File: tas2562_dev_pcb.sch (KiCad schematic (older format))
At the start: 24 parts, among them J1 Conn_01x10_Female, J2 ADDR, J3 Screw_Terminal_01x02, J4 Conn_01x10_Female, U1 LM1117-1.8, U2 TAS2562

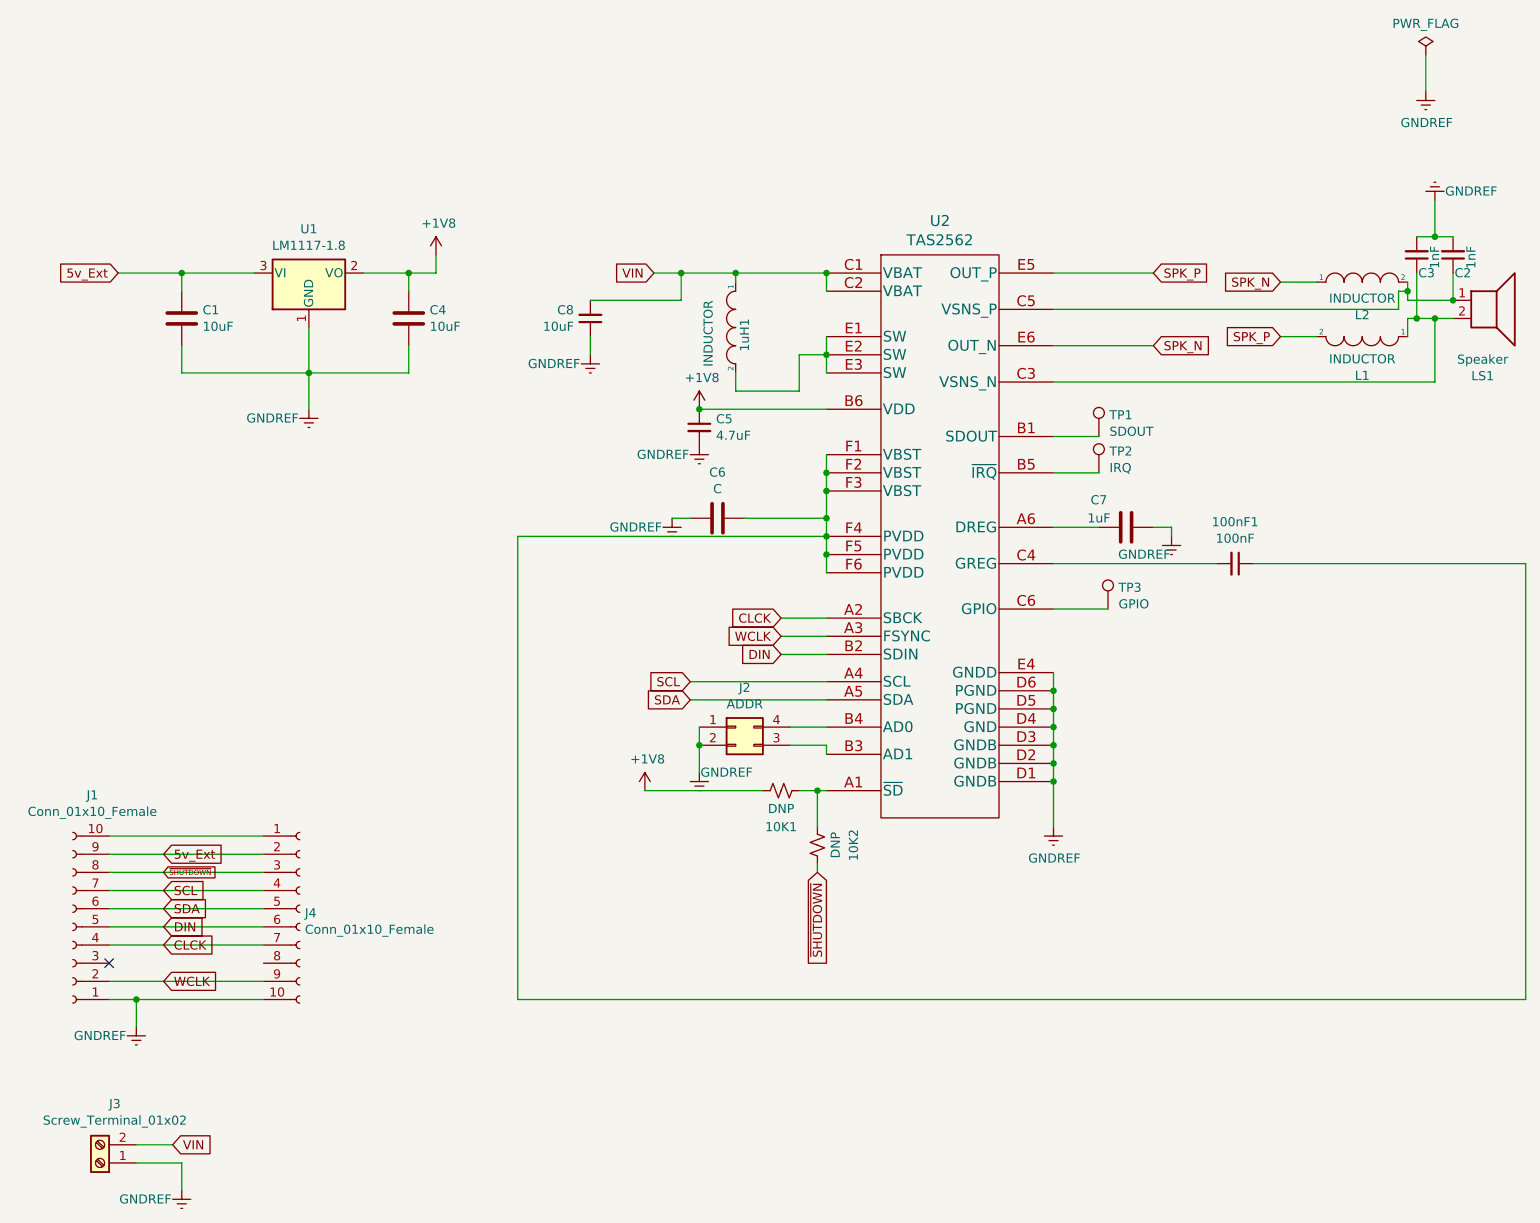
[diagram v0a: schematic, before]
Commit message: added gerber, layout done in 2layers
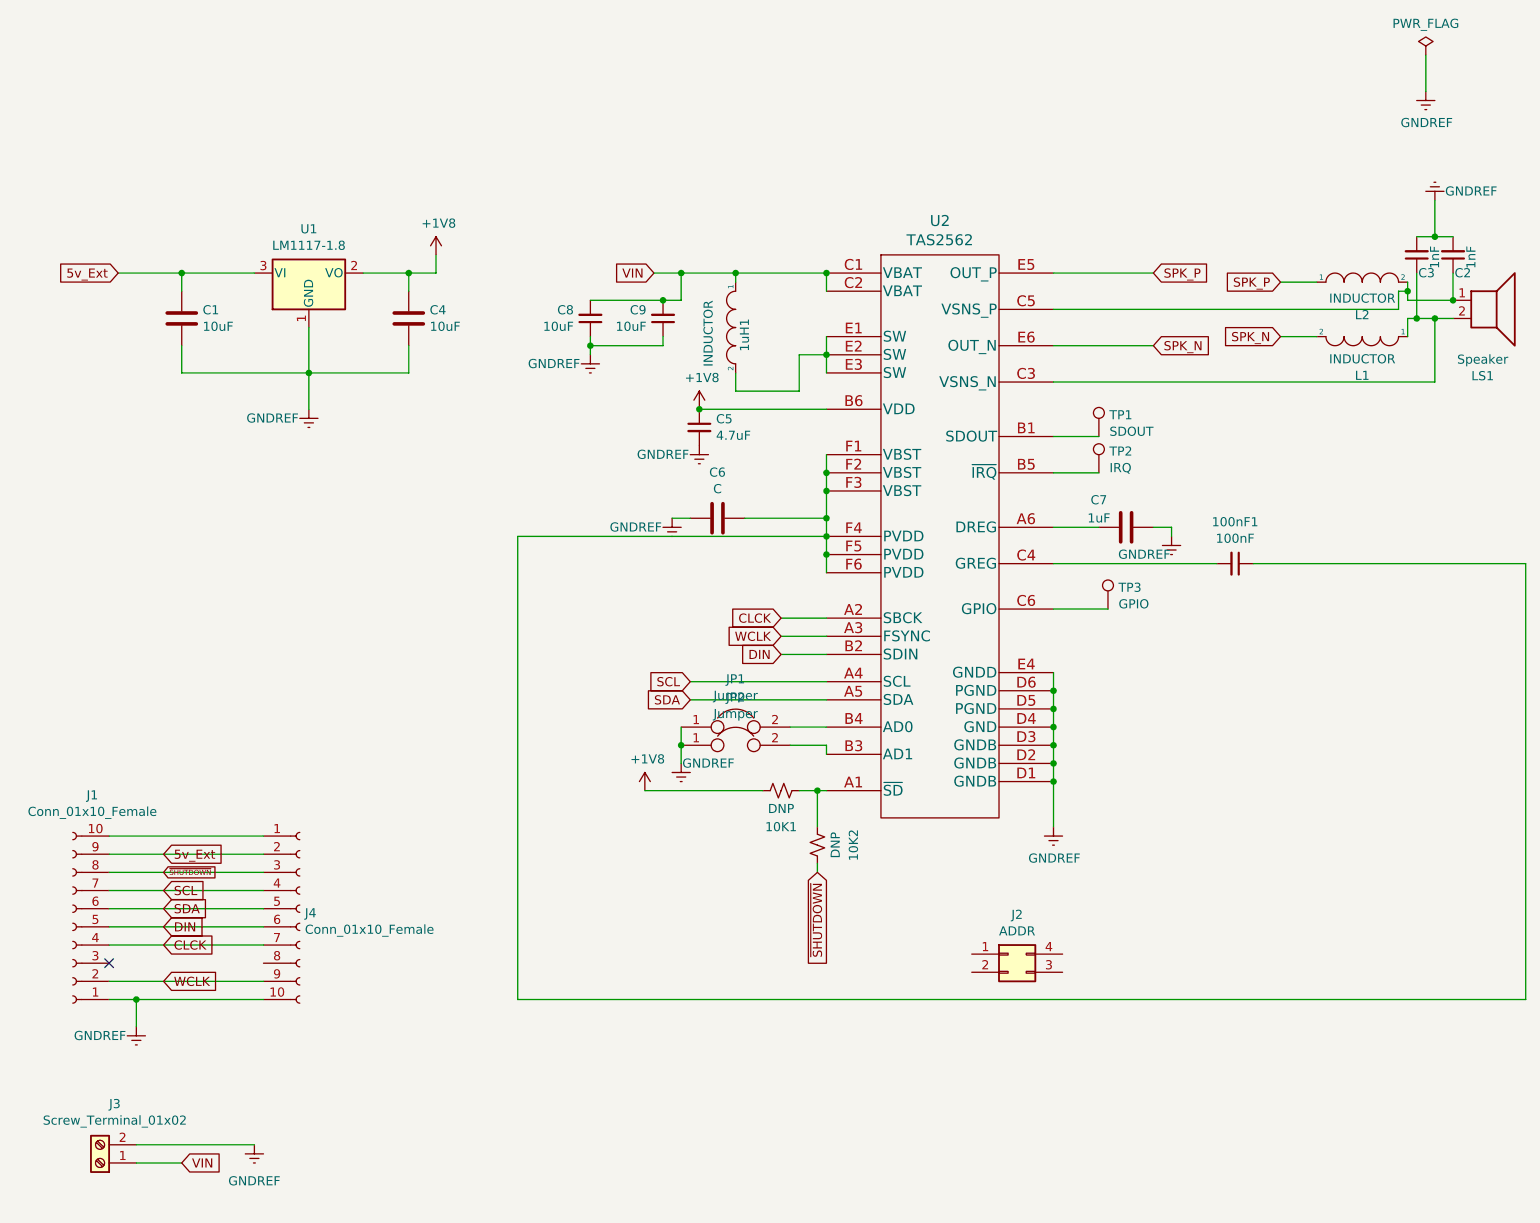
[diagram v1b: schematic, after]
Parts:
- added C9: 10uF, Capacitor_SMD:C_0805_2012Metric, symbol Device:C_Small
- added JP1, JP2: Jumper, Jumper:SolderJumper-2_P1.3mm_Open_TrianglePad1.0x1.5mm, symbol Device:Jumper
- 1uH1: footprint Inductor_SMD:1212_wurth -> Inductor_SMD:6.6-6.4
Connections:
- net GNDREF: now also J3.2 (Pin_2), C9.1, JP1.1, JP2.1; no longer J2.1 (Pin_1), J2.2 (Pin_2), J3.1 (Pin_1)
- net SPK_N: now also L1.2; no longer L2.1
- net SPK_P: now also L2.1; no longer L1.2
- net VIN: now also J3.1 (Pin_1), C9.2; no longer J3.2 (Pin_2)
- net at U2.B3 (AD1): now also JP2.2; no longer J2.3 (Pin_3)
- net at U2.B4 (AD0): now also JP1.2; no longer J2.4 (Pin_4)
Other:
- moved on the sheet: J2
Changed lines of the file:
@@
 	-1   0    0    1
 $EndComp
+Text GLabel 7700 2300 0    50   Input ~ 0
+SPK_P
 Text GLabel 7700 2600 0    50   Input ~ 0
-SPK_P
-Text GLabel 7700 2300 0    50   Input ~ 0
 SPK_N
 Wire Wire Line
@@
 Text GLabel 7000 2250 2    50   Input ~ 0
 SPK_P
-Text GLabel 7000 2650 2    50   Input ~ 0
-SPK_N
 Wire Wire Line
 	7000 2650 6450 2650
@@
 F 0 "1uH1" H 4650 2500 50  0000 L CNN
 F 1 "INDUCTOR" H 4550 2700 50  0000 L CNN
-F 2 "Inductor_SMD:1212_wurth" H 4700 2550 50  0001 C CNN
+F 2 "Inductor_SMD:6.6-6.4" H 4700 2550 50  0001 C CNN
 F 3 "~" H 4700 2550 50  0001 C CNN
 	1    4700 2550
@@
 L Connector_Generic:Conn_02x02_Counter_Clockwise J2
 U 1 1 5CEA5842
-P 4700 4750
-F 0 "J2" H 4750 4967 50  0000 C CNN
-F 1 "ADDR" H 4750 4876 50  0000 C CNN
-F 2 "Connector_PinHeader_2.54mm:PinHeader_2x02_P2.54mm_Vertical" H 4700 4750 50  0001 C CNN
-F 3 "~" H 4700 4750 50  0001 C CNN
-	1    4700 4750
+P 6200 6000
+F 0 "J2" H 6250 6217 50  0000 C CNN
+F 1 "ADDR" H 6250 6126 50  0000 C CNN
+F 2 "Connector_PinHeader_2.54mm:PinHeader_2x02_P2.54mm_Vertical" H 6200 6000 50  0001 C CNN
+F 3 "~" H 6200 6000 50  0001 C CNN
+	1    6200 6000
 	1    0    0    -1
 $EndComp
@@
 Wire Wire Line
 	5200 4850 5200 4900
-Wire Wire Line
-	4500 4750 4500 4850
-Connection ~ 4500 4850
-Wire Wire Line
-	4500 4850 4500 5000
 Text GLabel 4950 4150 0    50   Input ~ 0
 CLCK
@@
 L power:GNDREF #PWR0106
 U 1 1 5CF31996
-P 4500 5000
-F 0 "#PWR0106" H 4500 4750 50  0001 C CNN
-F 1 "GNDREF" H 4650 5000 50  0000 C CNN
-F 2 "" H 4500 5000 50  0001 C CNN
-F 3 "" H 4500 5000 50  0001 C CNN
-	1    4500 5000
+P 4400 4950
+F 0 "#PWR0106" H 4400 4700 50  0001 C CNN
+F 1 "GNDREF" H 4550 4950 50  0000 C CNN
+F 2 "" H 4400 4950 50  0001 C CNN
+F 3 "" H 4400 4950 50  0001 C CNN
+	1    4400 4950
 	1    0    0    -1
 $EndComp
@@
 	-1   0    0    1
 $EndComp
-Text GLabel 1600 7050 2    50   Input ~ 0
+Text GLabel 1650 7150 2    50   Input ~ 0
 VIN
-Wire Wire Line
-	1400 7050 1600 7050
 $Comp
 L power:GNDREF #PWR0114
 U 1 1 5CFAE4D4
-P 1650 7300
-F 0 "#PWR0114" H 1650 7050 50  0001 C CNN
-F 1 "GNDREF" H 1450 7250 50  0000 C CNN
-F 2 "" H 1650 7300 50  0001 C CNN
-F 3 "" H 1650 7300 50  0001 C CNN
-	1    1650 7300
+P 2050 7050
+F 0 "#PWR0114" H 2050 6800 50  0001 C CNN
+F 1 "GNDREF" H 2050 6850 50  0000 C CNN
+F 2 "" H 2050 7050 50  0001 C CNN
+F 3 "" H 2050 7050 50  0001 C CNN
+	1    2050 7050
 	1    0    0    -1
 $EndComp
 Wire Wire Line
 	1400 7150 1650 7150
-Wire Wire Line
-	1650 7150 1650 7300
 $Comp
 L Connector:Conn_01x10_Female J4
@@
 $EndComp
 Wire Wire Line
-	3900 2400 4400 2400
+	3900 2400 4300 2400
 Wire Wire Line
 	4400 2400 4400 2250
@@
 $EndComp
 Wire Wire Line
-	3900 2700 3900 2600
+	3900 2700 3900 2650
 Wire Wire Line
 	8500 1050 8500 1250
@@
 Wire Wire Line
 	8650 2250 8650 2400
+$Comp
+L Device:Jumper JP1
+U 1 1 5CEB9F24
+P 4700 4750
+F 0 "JP1" H 4700 5014 50  0000 C CNN
+F 1 "Jumper" H 4700 4923 50  0000 C CNN
+F 2 "Jumper:SolderJumper-2_P1.3mm_Open_TrianglePad1.0x1.5mm" H 4700 4750 50  0001 C CNN
+F 3 "~" H 4700 4750 50  0001 C CNN
+	1    4700 4750
+	1    0    0    -1
+$EndComp
+$Comp
+L Device:Jumper JP2
+U 1 1 5CEBC5CC
+P 4700 4850
+F 0 "JP2" H 4700 5114 50  0000 C CNN
+F 1 "Jumper" H 4700 5023 50  0000 C CNN
+F 2 "Jumper:SolderJumper-2_P1.3mm_Open_TrianglePad1.0x1.5mm" H 4700 4850 50  0001 C CNN
+F 3 "~" H 4700 4850 50  0001 C CNN
+	1    4700 4850
+	1    0    0    -1
+$EndComp
+Wire Wire Line
+	4400 4750 4400 4850
+Connection ~ 4400 4850
+Wire Wire Line
+	4400 4850 4400 4950
+Wire Wire Line
+	1400 7050 2050 7050
+Text GLabel 7000 2650 2    50   Input ~ 0
+SPK_N
+$Comp
+L Device:C_Small C9
+U 1 1 5CEFB0AD
+P 4300 2500
+F 0 "C9" H 4209 2454 50  0000 R CNN
+F 1 "10uF" H 4209 2545 50  0000 R CNN
+F 2 "Capacitor_SMD:C_0805_2012Metric" H 4300 2500 50  0001 C CNN
+F 3 "~" H 4300 2500 50  0001 C CNN
+	1    4300 2500
+	1    0    0    1
+$EndComp
+Connection ~ 4300 2400
+Wire Wire Line
+	4300 2400 4400 2400
+Wire Wire Line
+	3900 2650 4300 2650
+Wire Wire Line
+	4300 2650 4300 2600
+Connection ~ 3900 2650
+Wire Wire Line
+	3900 2650 3900 2600
 $EndSCHEMATC
